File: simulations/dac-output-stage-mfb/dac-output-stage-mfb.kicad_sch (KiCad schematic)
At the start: 16 parts, among them U1 RRIO_OPAMP

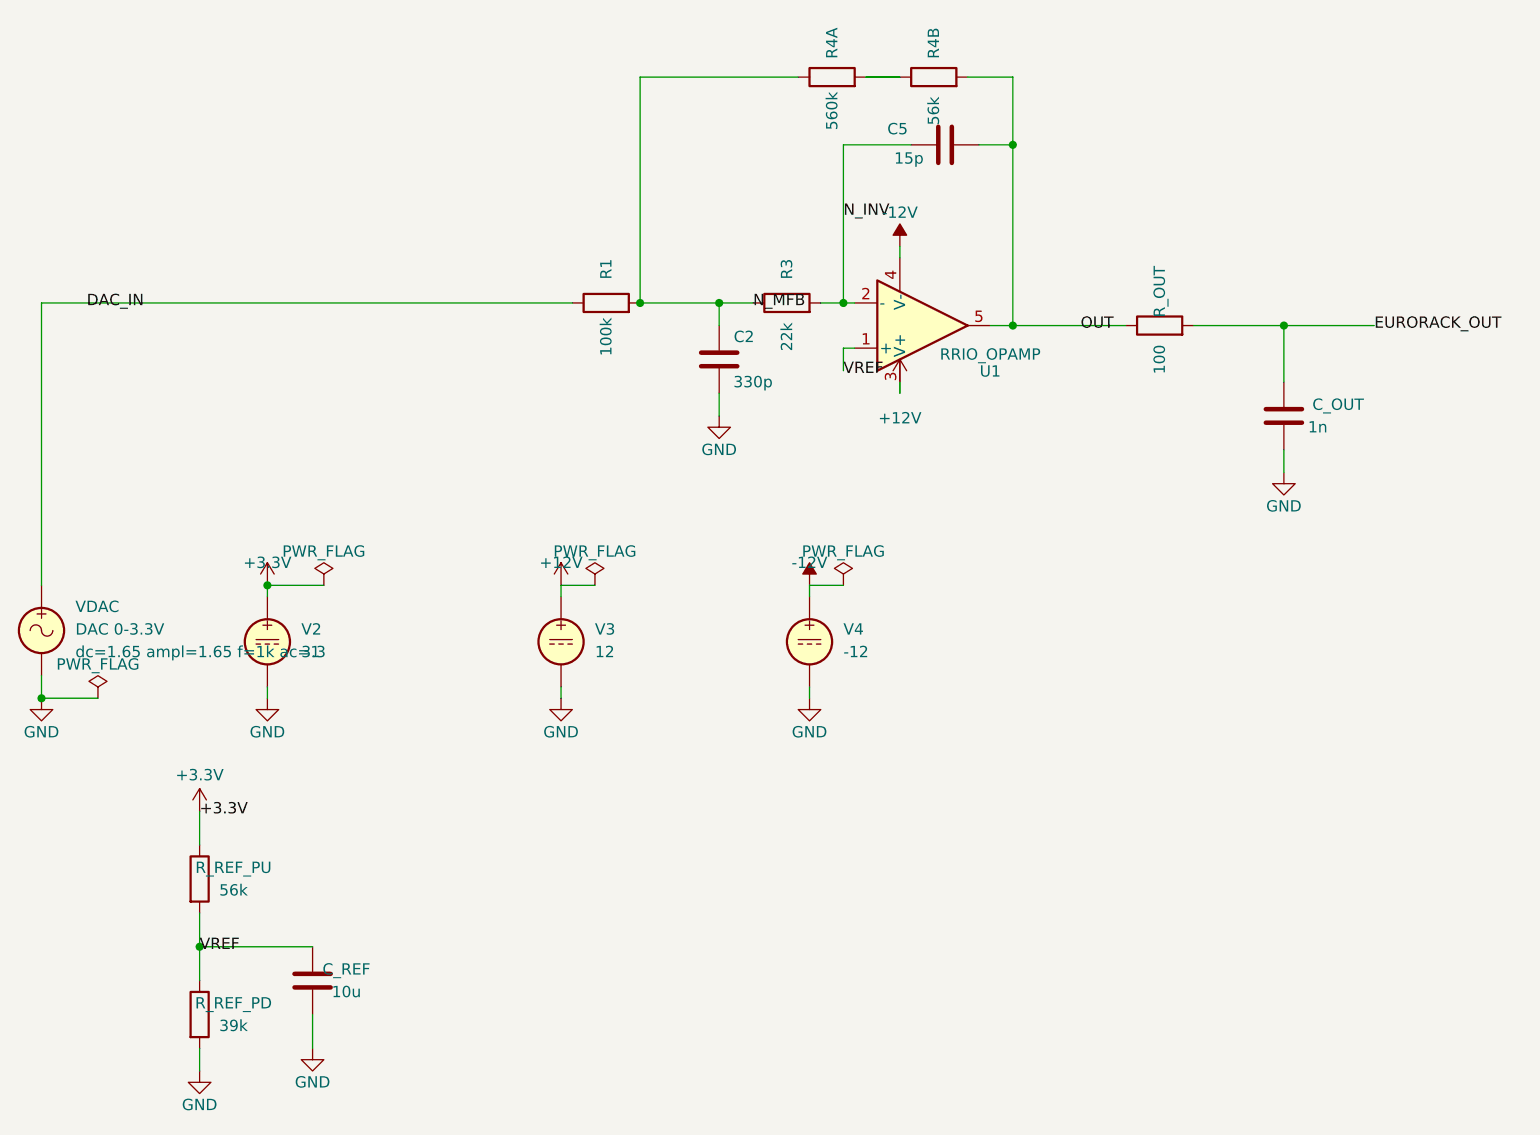
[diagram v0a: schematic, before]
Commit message: Simplified feedback loop.
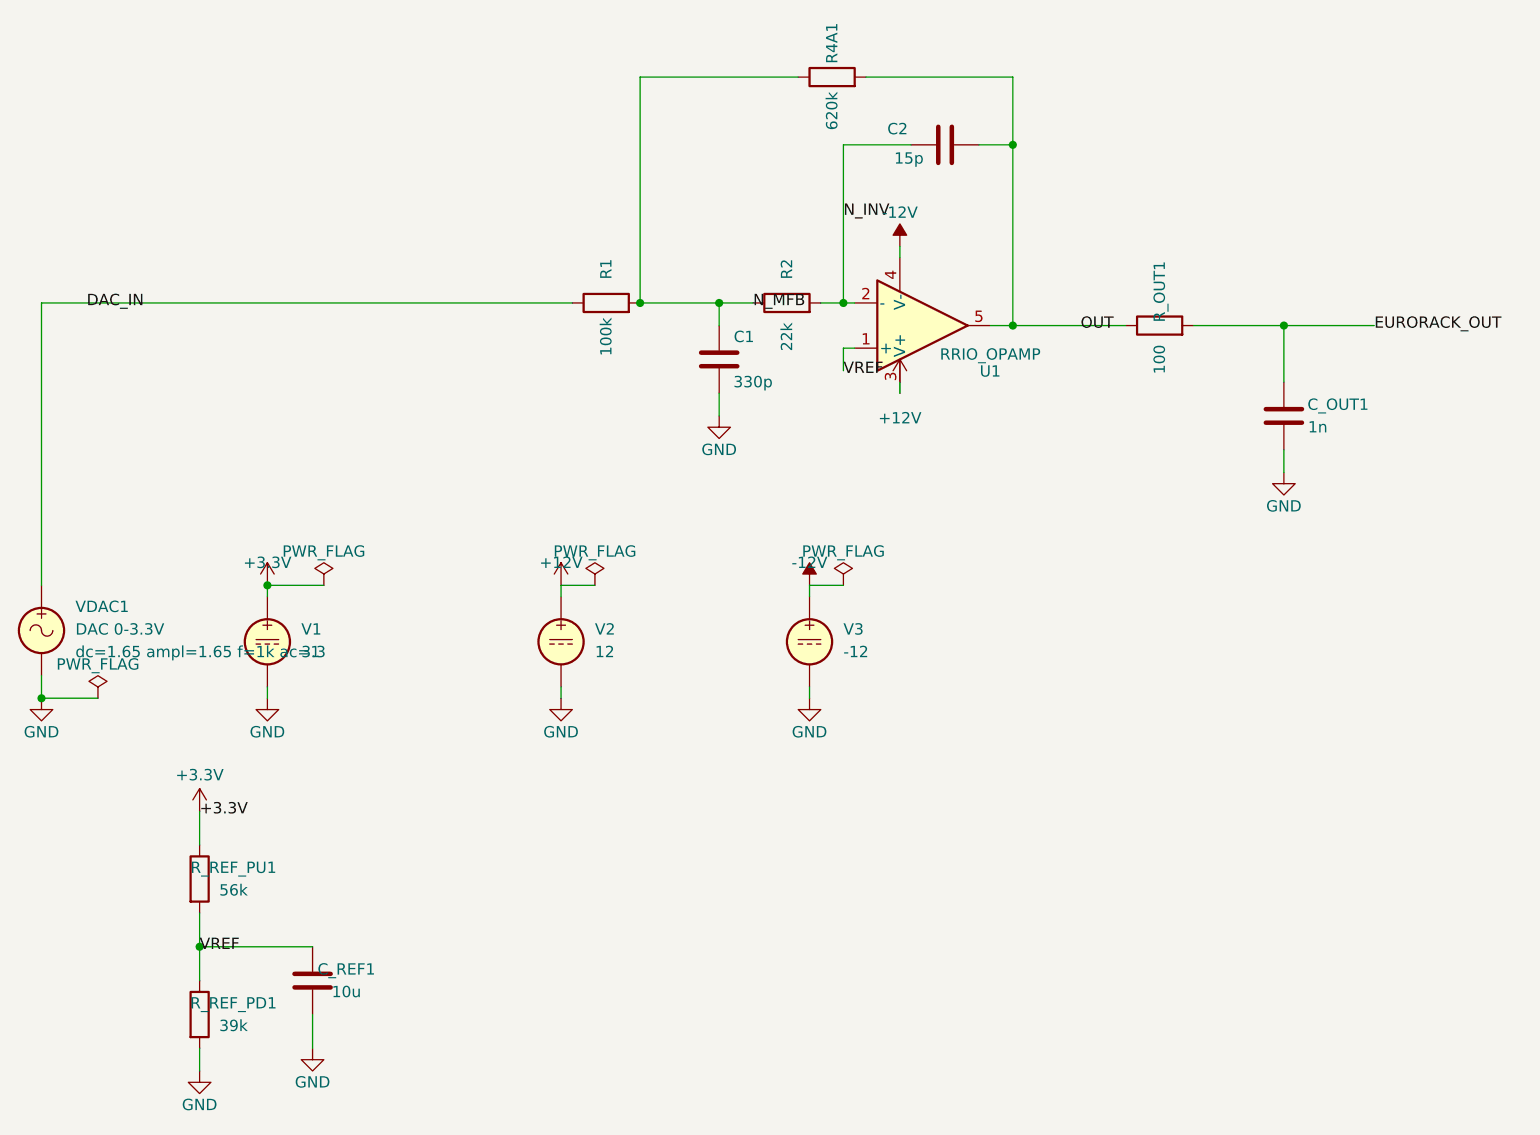
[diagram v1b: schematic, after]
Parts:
- removed R4B: 56k, symbol Device:R
- R4A1: renamed from R4A; value 560k -> 620k
- renumbered C2 to C1, C5 to C2, C_OUT to C_OUT1, C_REF to C_REF1, R3 to R2, R_OUT to R_OUT1, R_REF_PD to R_REF_PD1, R_REF_PU to R_REF_PU1, V2 to V1, V3 to V2, V4 to V3, VDAC to VDAC1
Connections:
- net OUT: now also R4A1.2

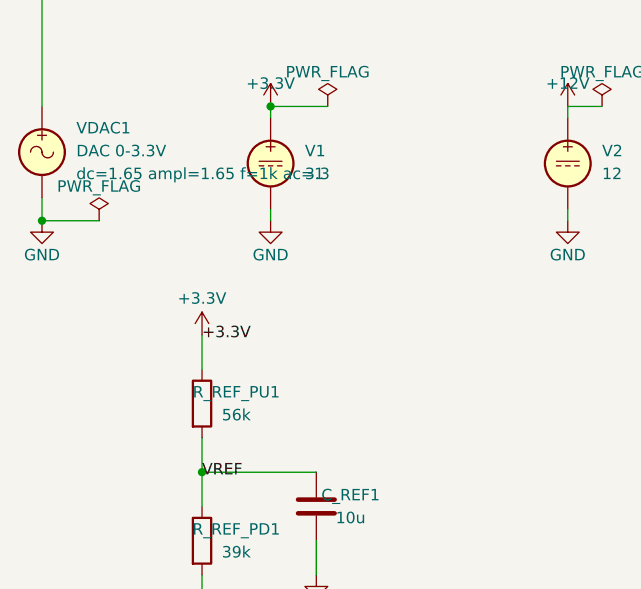
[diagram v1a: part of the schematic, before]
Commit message: Output DC center fixed at ~0V
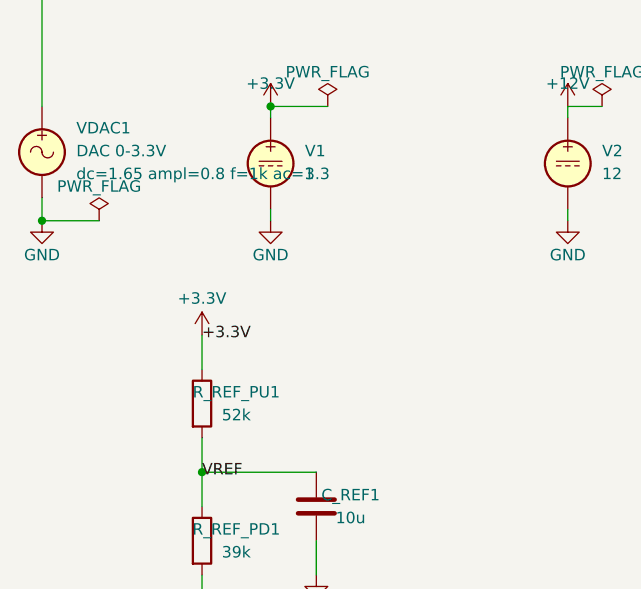
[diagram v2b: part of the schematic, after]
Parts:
- R_REF_PU1: value 56k -> 52k
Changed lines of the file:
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@@
 			)
 		)
-		(property "Sim.Params" "dc=1.65 ampl=1.65 f=1k ac=1"
+		(property "Sim.Params" "dc=1.65 ampl=0.8 f=1k ac=1"
 			(at 29.21 115.4401 0)
 			(show_name no)
@@
 			)
 		)
-		(property "Value" "56k"
+		(property "Value" "52k"
 			(at 46.99 142.24 0)
 			(show_name no)
